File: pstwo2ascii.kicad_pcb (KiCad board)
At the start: 2 copper layers, 58.7 x 56.2 mm, 34 parts, among them J1 ASCII, J2 PS2, J3 XT, J4 RS232 v24, J5 Control, J6 USB-C Power, J7 SPI, SW1 RESET, SW2 MODE, SW3 CONFIG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

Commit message: Improvements. Added 3D models, changed pushbuttons to slider switches. Clearer text.
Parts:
- SW2, SW3: footprint Sporos_Tech_Footprints:SW_SPST_Omron_B3FS-100xP_4P -> Sporos_Tech_Footprints:CL-SB-12B-0x SPDT switch
- moved SW2 1.19 mm to (23.9, 34.9), turned to -90 degrees
- moved SW3 0.58 mm to (23.9, 47.7), turned to -90 degrees
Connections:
- SW2 pad 1: ~{MODE} -> unconnected-(SW2-A-Pad1)
- SW2 pad 2: unconnected-(SW2-Pad2) -> ~{MODE}
- SW3 pad 1: ~{CONFIG} -> unconnected-(SW3-A-Pad1)
- SW3 pad 2: unconnected-(SW3-Pad2) -> ~{CONFIG}
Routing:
- net ~{CONFIG}: track 52.8 -> 45.9 mm
- net ~{MODE}: track 62.9 -> 66.1 mm
- net GND: track 29.7 -> 29.0 mm
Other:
- board text added: "DEV"
- board text added: "HOST"
- board text added: "OFF"
- board text added: "ON"
- board text added: "Sporos Tech"
- board text removed: "© 2025 Sporos Tech"

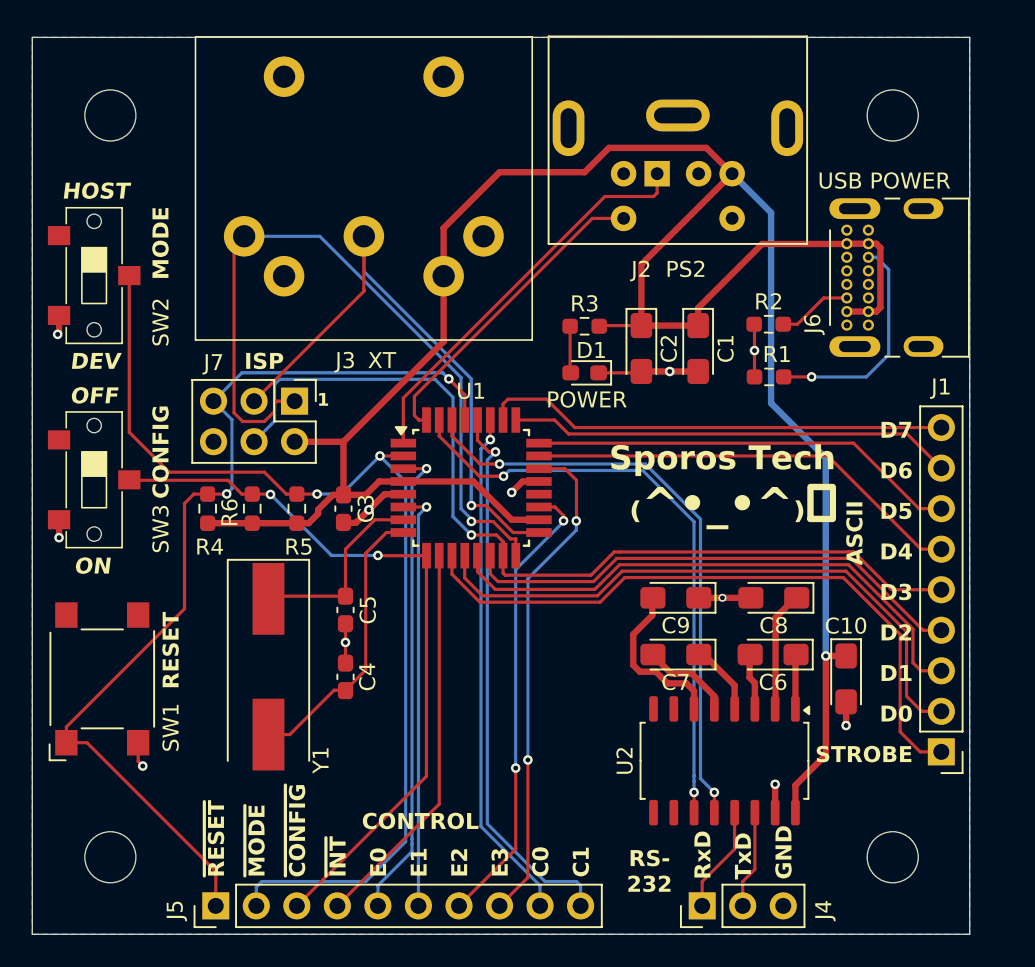
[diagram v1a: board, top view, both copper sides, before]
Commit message: Add a few extra GND pins on the pin connectors. Also added copyright information in the sheets. Also updated pretty files.
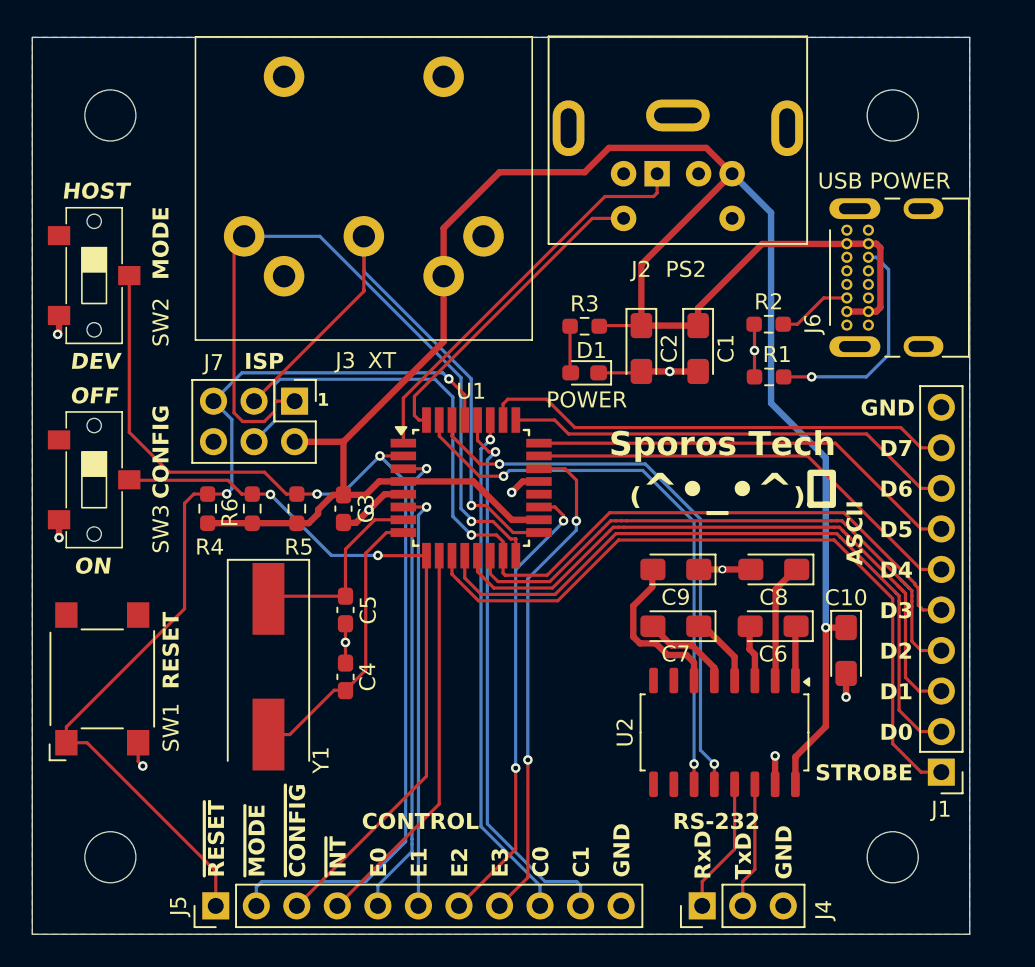
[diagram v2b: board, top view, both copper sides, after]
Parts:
- J1: footprint Connector_PinHeader_2.54mm:PinHeader_1x09_P2.54mm_Vertical -> Connector_PinHeader_2.54mm:PinHeader_1x10_P2.54mm_Vertical
- J5: footprint Connector_PinHeader_2.54mm:PinHeader_1x10_P2.54mm_Vertical -> Connector_PinHeader_2.54mm:PinHeader_1x11_P2.54mm_Vertical
- moved C10 1.78 mm to (71.0, 58.4)
- moved C6 1.78 mm to (66.4, 56.9)
- moved C7 1.78 mm to (60.3, 56.9)
- moved C8 1.78 mm to (66.5, 53.3)
- moved C9 1.78 mm to (60.3, 53.3)
- moved U2 1.78 mm to (63.4, 63.6)
- moved J1 1.27 mm to (77.0, 66.0)
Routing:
- net D2: track 32.1 -> 36.4 mm
- net D1: track 35.1 -> 39.4 mm
- net D0: track 38.4 -> 42.6 mm
- net STROBE: track 41.3 -> 45.4 mm
- net D3/MOSI: track 58.2 -> 61.5 mm
- net /V24_RxD: track 6.68 -> 8.46 mm
- net VCC: track 149.5 -> 147.7 mm
- net RxD: track 37.5 -> 35.7 mm
- net /V24_TxD: track 6.16 -> 7.94 mm
- net TxD: track 37.7 -> 36.1 mm
- net D4: track 27.6 -> 28.2 mm
- net D7: track 29.3 -> 29.9 mm
- net D6: track 27.9 -> 28.4 mm
- net D5: track 26.9 -> 27.4 mm
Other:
- board text added: "RS-232"
- board text removed: "RS- 232"

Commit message: Some small improvements, and assigning datasheets.
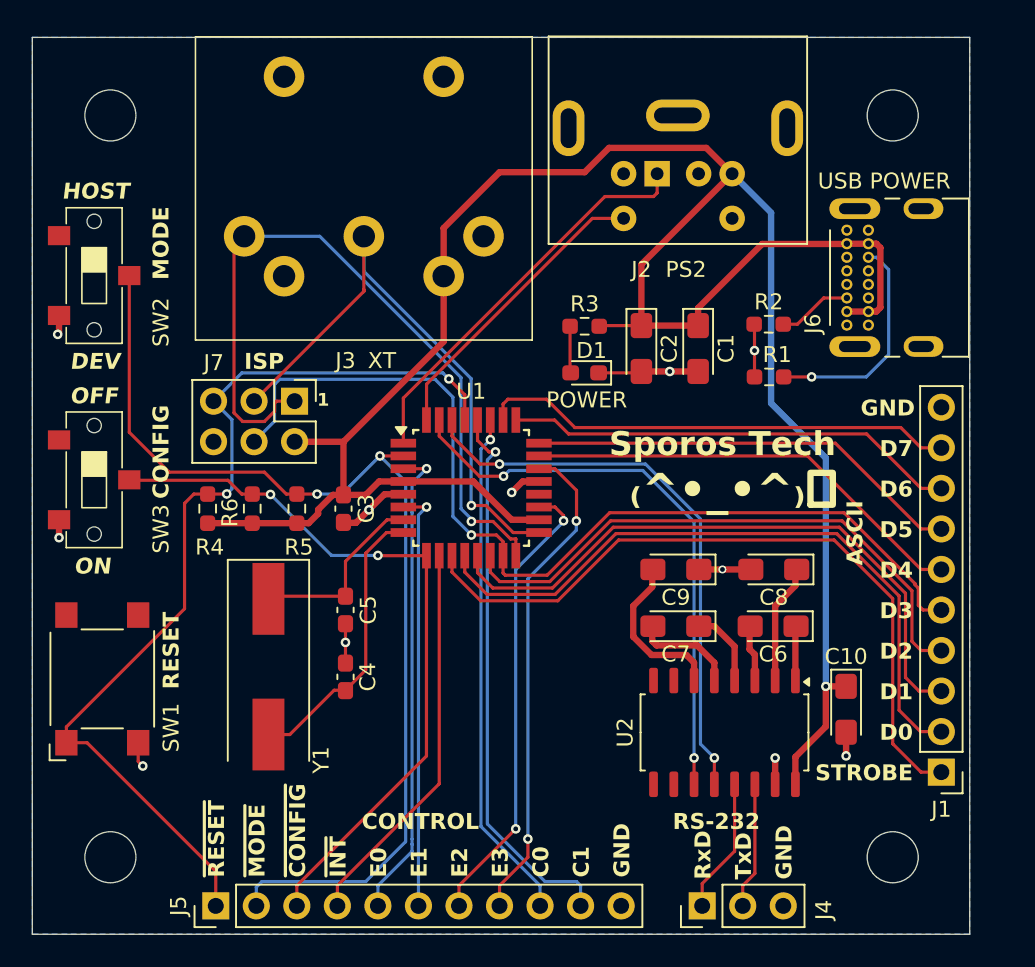
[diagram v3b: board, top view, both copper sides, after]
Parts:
- U1: value ATmega328PB-A -> ATmega328-AU
- moved C10 3.68 mm to (71.0, 62.1)
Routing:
- net PS2_CLK: track 19.8 -> 18.9 mm
- net Net-(U2-C2-): track 5.77 -> 6.51 mm

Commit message: Some final tweaks, changing the labels of the buttons and switches.
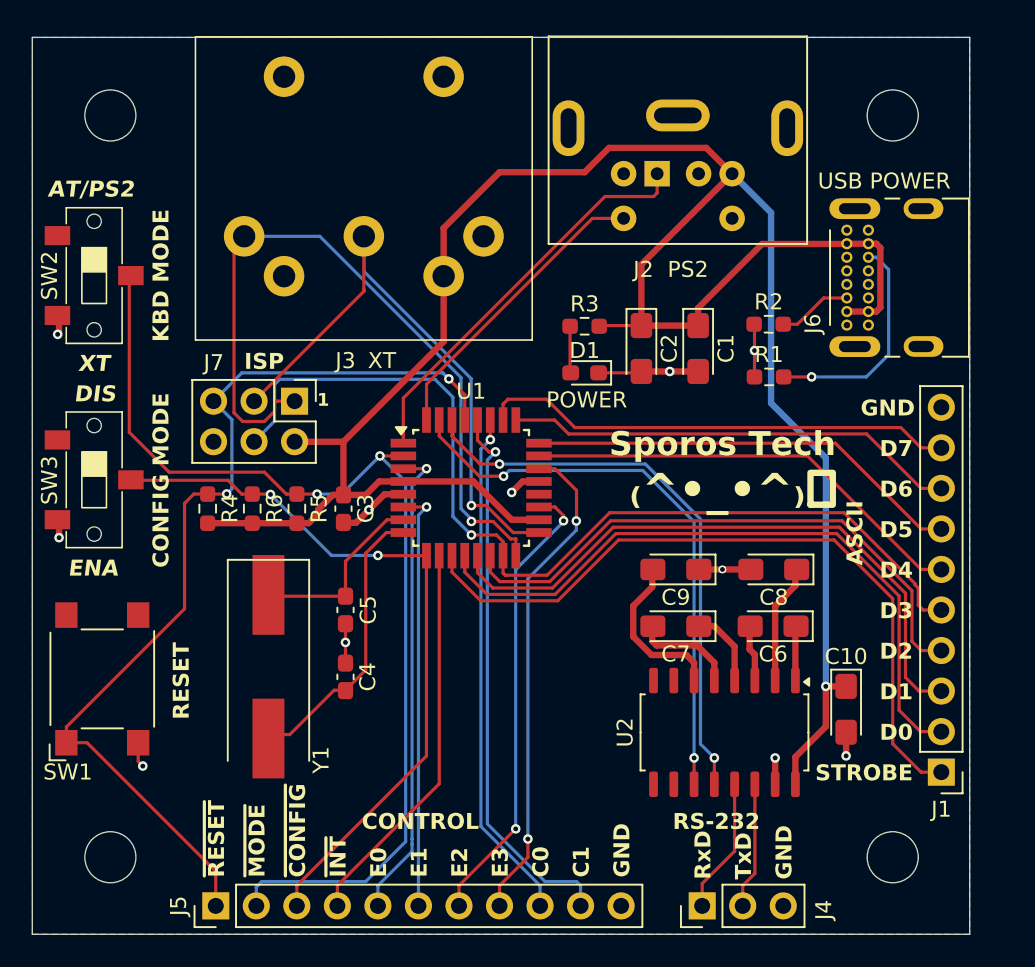
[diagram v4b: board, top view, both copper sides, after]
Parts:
- SW2: value MODE -> KBD MODE
- SW3: value CONFIG -> CONFIG MODE
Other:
- board text added: "AT/PS2"
- board text added: "DIS"
- board text added: "ENA"
- board text added: "XT"
- board text removed: "DEV"
- board text removed: "HOST"
- board text removed: "OFF"
- board text removed: "ON"
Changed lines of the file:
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@@
 		)
 		(pad "1" smd rect
-			(at -4.25 0 270)
-			(size 4.5 2)
+			(at -4.5 0 270)
+			(size 5 2)
 			(layers "F.Cu" "F.Mask" "F.Paste")
 			(net 46 "Net-(U1-XTAL1{slash}PB6)")
@@
 		)
 		(pad "2" smd rect
-			(at 4.25 0 270)
-			(size 4.5 2)
+			(at 4.5 0 270)
+			(size 5 2)
 			(layers "F.Cu" "F.Mask" "F.Paste")
 			(net 1 "Net-(U1-XTAL2{slash}PB7)")
@@
 		(tags "capacitor handsolder")
 		(property "Reference" "C3"
-			(at 0 -1.43 90)
+			(at 0 -1.397 90)
 			(layer "F.SilkS")
 			(effects
@@
 		(tags "resistor handsolder")
 		(property "Reference" "R4"
-			(at -2.413 0.127 180)
+			(at 0 1.397 270)
 			(layer "F.SilkS")
 			(effects
@@
 		(tags "resistor handsolder")
 		(property "Reference" "R1"
-			(at 0.508 -1.397 180)
+			(at 0 -1.397 180)
 			(layer "F.SilkS")
 			(effects
@@
 		(tags "resistor handsolder")
 		(property "Reference" "R6"
-			(at -0.254 -1.397 90)
+			(at 0 1.397 90)
 			(layer "F.SilkS")
 			(effects
@@
 		(tags "Tactile Switch")
 		(property "Reference" "SW1"
-			(at -3.048 4.318 90)
+			(at -5.842 -2.159 180)
 			(layer "F.SilkS")
 			(effects
@@
 		)
 		(property "Value" "RESET"
-			(at 1.778 4.318 90)
+			(at -0.127 4.953 90)
 			(layer "F.SilkS")
 			(effects
@@
 		(at 23.876 47.723 -90)
 		(property "Reference" "SW3"
-			(at 3.077 -4.191 90)
+			(at 0.029 2.794 90)
 			(unlocked yes)
 			(layer "F.SilkS")
@@
 			)
 		)
-		(property "Value" "CONFIG"
-			(at -1.749 -4.191 90)
+		(property "Value" "CONFIG MODE"
+			(at 0.029 -4.191 90)
 			(unlocked yes)
 			(layer "F.SilkS")
@@
 		)
 		(pad "1" smd rect
-			(at -2.5 2.2)
-			(size 1.4 1.2)
+			(at -2.5 2.3)
+			(size 1.6 1.2)
 			(layers "F.Cu" "F.Mask" "F.Paste")
 			(net 58 "unconnected-(SW3-A-Pad1)")
@@
 		)
 		(pad "2" smd rect
-			(at 0 -2.2)
-			(size 1.4 1.2)
+			(at 0 -2.3)
+			(size 1.6 1.2)
 			(layers "F.Cu" "F.Mask" "F.Paste")
 			(net 22 "~{CONFIG}")
@@
 		)
 		(pad "3" smd rect
-			(at 2.5 2.2)
-			(size 1.4 1.2)
+			(at 2.5 2.3)
+			(size 1.6 1.2)
 			(layers "F.Cu" "F.Mask" "F.Paste")
 			(net 2 "GND")
@@
 		(tags "mini din 6pin connector socket")
 		(property "Reference" "J2"
-			(at 0.986 -6.002 0)
+			(at 0.859 -6.002 0)
 			(layer "F.SilkS")
 			(effects
@@
 		)
 		(property "Value" "PS2"
-			(at -1.808 -6.002 0)
+			(at -1.935 -6.002 0)
 			(layer "F.SilkS")
 			(effects
@@
 		(tags "resistor handsolder")
 		(property "Reference" "R5"
-			(at -2.413 0.127 180)
+			(at 0 1.397 270)
 			(layer "F.SilkS")
 			(effects
@@
 		(at 23.876 34.925 -90)
 		(property "Reference" "SW2"
-			(at 2.921 -4.191 90)
+			(at 0 2.794 90)
 			(unlocked yes)
 			(layer "F.SilkS")
@@
 			)
 		)
-		(property "Value" "MODE"
-			(at -2.032 -4.191 90)
+		(property "Value" "KBD MODE"
+			(at 0 -4.191 90)
 			(unlocked yes)
 			(layer "F.SilkS")
@@
 		)
 		(pad "1" smd rect
-			(at -2.5 2.2)
-			(size 1.4 1.2)
+			(at -2.5 2.3)
+			(size 1.6 1.2)
 			(layers "F.Cu" "F.Mask" "F.Paste")
 			(net 57 "unconnected-(SW2-A-Pad1)")
@@
 		)
 		(pad "2" smd rect
-			(at 0 -2.2)
-			(size 1.4 1.2)
+			(at 0 -2.3)
+			(size 1.6 1.2)
 			(layers "F.Cu" "F.Mask" "F.Paste")
 			(net 17 "~{MODE}")
@@
 		)
 		(pad "3" smd rect
-			(at 2.5 2.2)
-			(size 1.4 1.2)
+			(at 2.5 2.3)
+			(size 1.6 1.2)
 			(layers "F.Cu" "F.Mask" "F.Paste")
 			(net 2 "GND")
@@
 		(tags "LED handsolder")
 		(property "Reference" "D1"
-			(at -0.43 1.397 0)
+			(at 0 1.397 0)
 			(layer "F.SilkS")
 			(effects
@@
 		)
 	)
-	(gr_text "ON"
-		(at 22.606 53.721 0)
+	(gr_text "ENA"
+		(at 22.225 53.848 0)
 		(layer "F.SilkS")
 		(effects
@@
 		)
 	)
-	(gr_text "HOST"
-		(at 21.844 30.226 0)
+	(gr_text "AT/PS2"
+		(at 20.955 30.099 0)
 		(layer "F.SilkS")
 		(effects
@@
 		)
 	)
-	(gr_text "OFF"
-		(at 22.352 43.053 0)
+	(gr_text "DIS"
+		(at 22.606 42.926 0)
 		(layer "F.SilkS")
 		(effects
@@
 		)
 	)
-	(gr_text "DEV"
-		(at 22.352 40.894 0)
+	(gr_text "XT"
+		(at 22.86 41.021 0)
 		(layer "F.SilkS")
 		(effects
@@
 		)
 	)
-	(gr_text_box "PS2Encoder\n© 2008-2018\nJim Brain &\nRETRO Innovations\n\npstwo2ascii\n© 2025\nPeter de Vroomen\nSporos Tech"
+	(gr_text_box "PS2Encoder\nCopyright 2008-2018\nJim Brain &\nRETRO Innovations\n\npstwo2ascii V1.0\nCopyright 2025\nPeter de Vroomen\nSporos Tech"
 		(start 41.783 55.1307)
 		(end 56.388 67.8053)
@@
 		(effects
 			(font
-				(size 0.8 0.8)
-				(thickness 0.16)
-				(bold yes)
+				(size 0.8 0.7)
+				(thickness 0.1)
 			)
 			(justify top)
